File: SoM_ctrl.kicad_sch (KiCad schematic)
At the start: 1 part, among them J2 Hermaphroditic_Molex_203456-0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

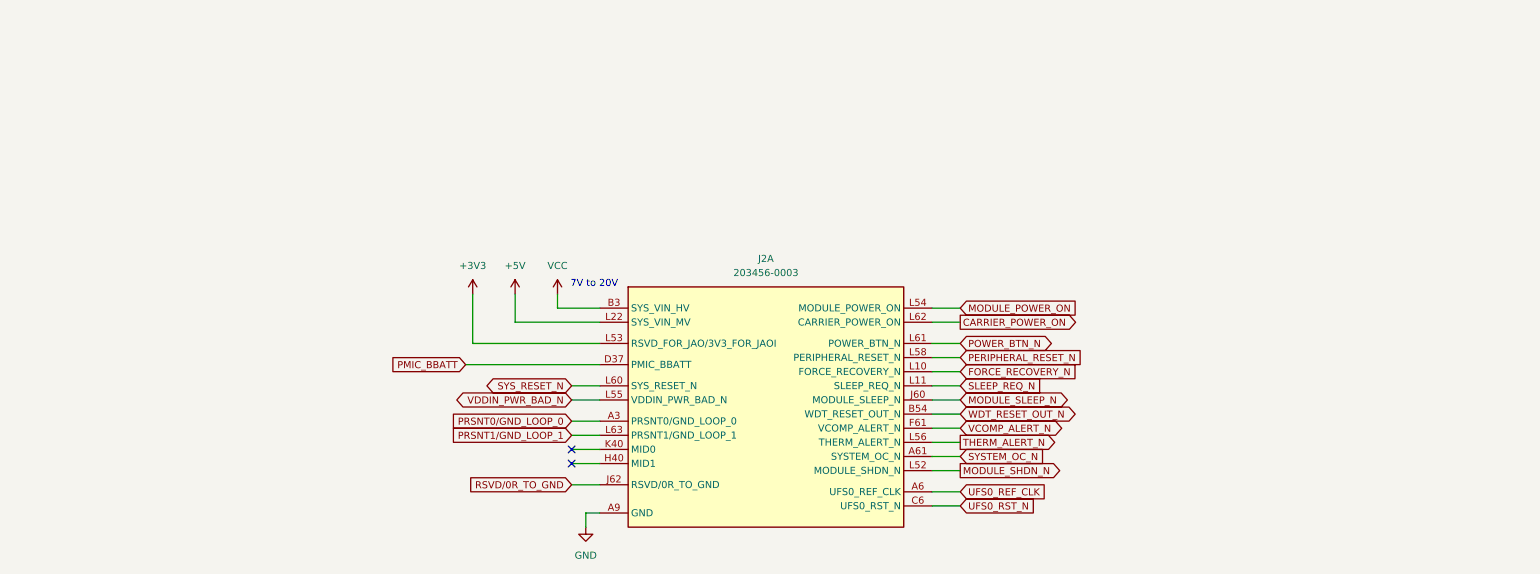
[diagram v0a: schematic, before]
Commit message: [#81778] Add decoupling capacitors
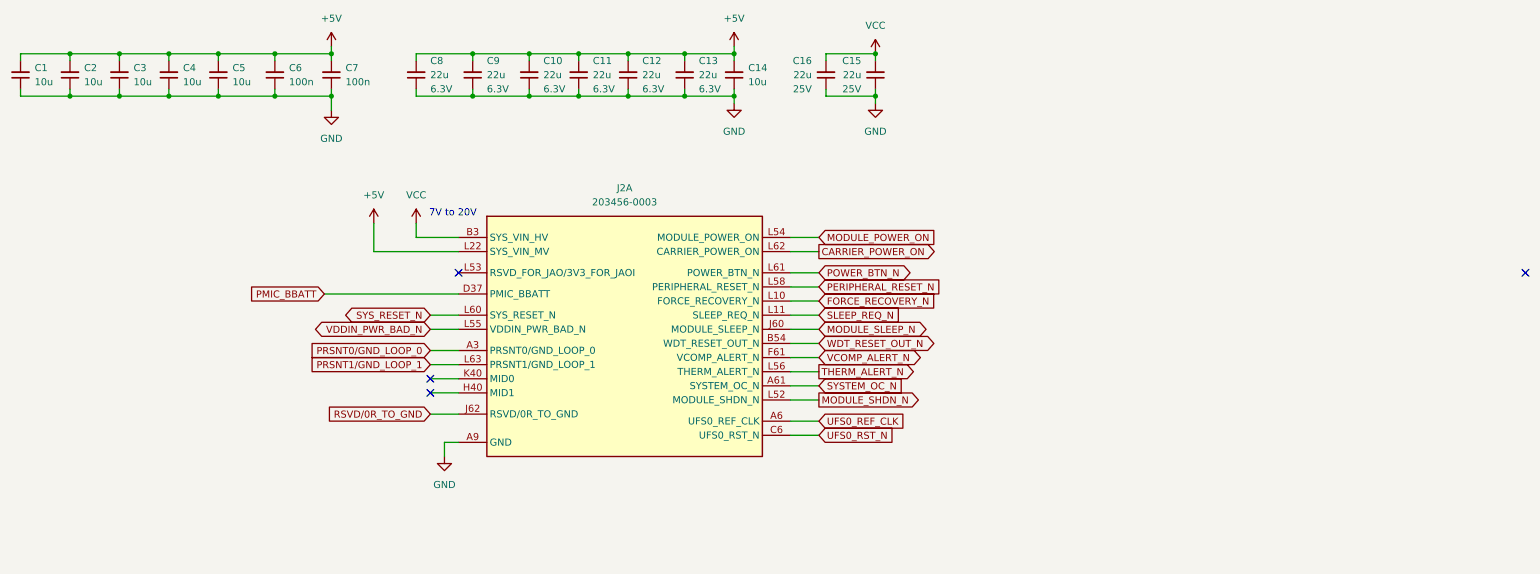
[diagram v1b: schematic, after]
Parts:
- added C1, C14, C2, C3, C4, C5: C_10u_0603, antmicro-footprints:C_0603_1608Metric, symbol antmicroCapacitors0603:C_10u_0603
- added C10, C11, C12, C13, C8, C9: C_22u_6.3V_X7R_0805, antmicro-footprints:C_0805_2012Metric, symbol antmicroCapacitorsmisc:C_22u_6.3V_X7R_0805
- added C15, C16: C_22u_25V_0805, antmicro-footprints:C_0805_2012Metric, symbol antmicroCapacitorsmisc:C_22u_25V_0805
- added C6, C7: C_100n_16V_X7R_0402, antmicro-footprints:C_0402_1005Metric, symbol antmicroCapacitors0402:C_100n_16V_X7R_0402
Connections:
- net +5V: now also C1.2, C10.2, C11.2, C12.2, C13.2, C14.2, C2.2, C3.2, C4.2, C5.2, C6.2, C7.2, C8.2, C9.2
- net GND: now also C1.1, C10.1, C11.1, C12.1, C13.1, C14.1, C15.1, C16.1, C2.1, C3.1, C4.1, C5.1, C6.1, C7.1, C8.1, C9.1
- net SYS_VIN_HV: now also C15.2, C16.2
- net +3V3: no longer names the net of J2.L53 (RSVD_FOR_JAO/3V3_FOR_JAOI)
- no-connect marks 2 -> 4
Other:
- moved on the sheet: J2A

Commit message: [#81778] Add 0R resistors
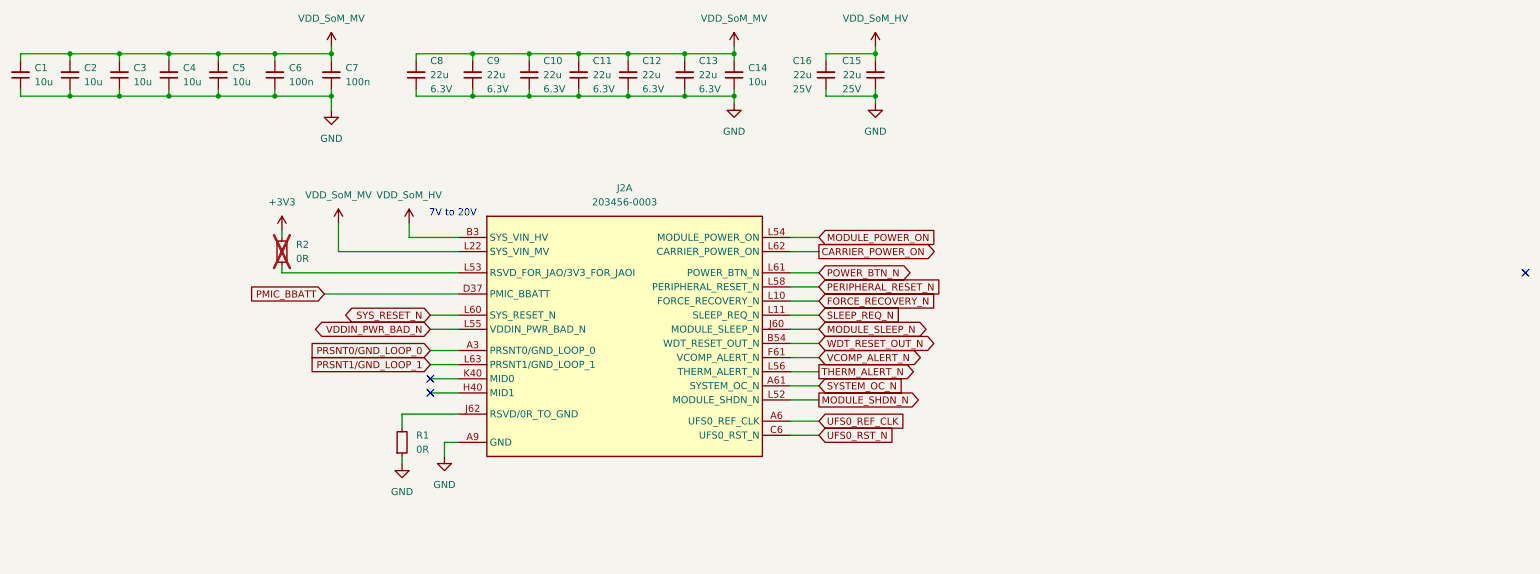
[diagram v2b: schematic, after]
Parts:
- added R1: R_0R_0402, antmicro-footprints:R_0402_1005Metric, symbol antmicroResistors0402:R_0R_0402
- added R2: R_0R_0603, antmicro-footprints:R_0603_1608Metric, symbol antmicroResistors0603:R_0R_0603
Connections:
- net GND: now also R1.1
- net at J2.L53 (RSVD_FOR_JAO/3V3_FOR_JAOI): now also R2.1
- net +5V renamed SYS_VIN_MV
- net RSVD/0R_TO_GND: no longer names the net of J2.J62 (RSVD/0R_TO_GND)
- net RSVD/0R_TO_GND: now also R1.2
- new net +3V3: R2.2
- no-connect marks 4 -> 3
